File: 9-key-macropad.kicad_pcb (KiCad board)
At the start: 2 copper layers, 20 parts, among them SW1 SW_Push, SW2 SW_Push, SW3 SW_Push, SW4 SW_Push, SW5 SW_Push, SW6 SW_Push, SW7 SW_Push, SW8 SW_Push, SW9 SW_Push, U1 XIAO-RP2040-DIP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

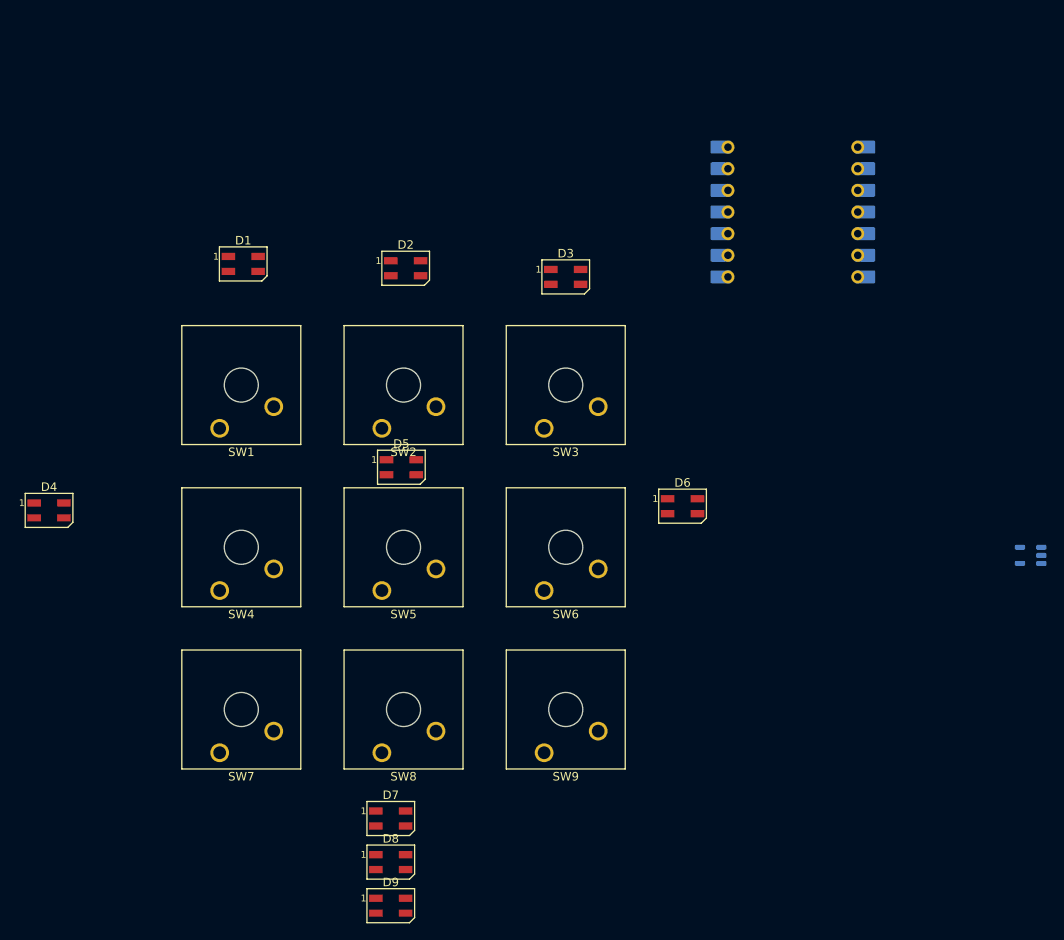
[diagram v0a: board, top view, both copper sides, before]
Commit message: Update switch and LED positions on PCB
Repositioned Cherry MX switches and SK6812MINI LEDs to new coordinates and orientations on the 9-key macropad PCB. This change likely reflects a new layout or mechanical design for improved ergonomics or aesthetics.
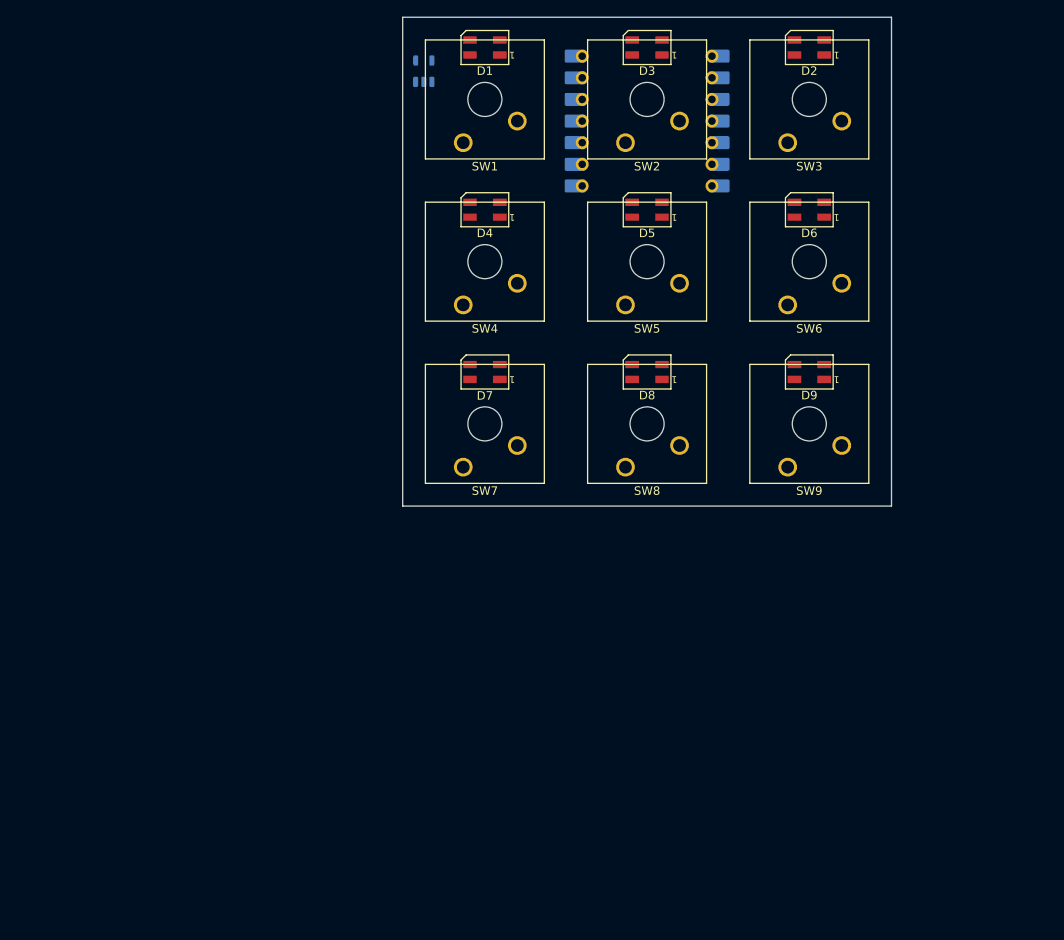
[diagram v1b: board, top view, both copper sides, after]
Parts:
- moved U2 91.2 mm to (72.2, 77.4), turned to 90 degrees
- moved D9 79.7 mm to (117.5, 112.8), turned to 180 degrees
- moved D8 65.0 mm to (98.5, 112.8), turned to 180 degrees
- moved D4 62.2 mm to (79.4, 93.7), turned to 180 degrees
- moved D2 54.0 mm to (117.5, 74.7), turned to 180 degrees
- moved D7 53.6 mm to (79.4, 112.8), turned to 180 degrees
- moved SW1 44.1 mm to (76.9, 85.8)
- moved SW4 44.1 mm to (76.9, 104.9)
- moved SW2 44.1 mm to (95.9, 85.8)
- moved SW3 44.1 mm to (115.0, 85.8)
- moved SW5 44.1 mm to (95.9, 104.9)
- moved SW6 44.1 mm to (115.0, 104.9)
- moved SW7 44.1 mm to (76.9, 123.9)
- moved SW8 44.1 mm to (95.9, 123.9)
- moved SW9 44.1 mm to (115.0, 123.9)
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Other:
- board outline added: 57.4 x 57.4 mm

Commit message: Rearrange key switches and LEDs, update net assignments
Moved key switches and SK6812MINI LEDs to new positions for improved layout. Updated net assignments for GPIO pins to match new key mapping and corrected NEOPIX and unconnected net references. Adjusted footprint locations for U1 and U2 to align with the new design.
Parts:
- moved SW1 19.6 mm to (78.1, 105.4)
- moved SW2 19.6 mm to (97.1, 105.4)
- moved SW3 19.6 mm to (116.2, 105.4)
- moved SW7 19.6 mm to (78.1, 143.5)
- moved SW8 19.6 mm to (97.1, 143.5)
- moved SW9 19.6 mm to (116.2, 143.5)
- moved D1 19.6 mm to (80.6, 94.2)
- moved D2 19.6 mm to (118.7, 94.2)
- moved D3 19.6 mm to (99.7, 94.2)
- moved D4 19.6 mm to (80.6, 113.2)
- moved D5 19.6 mm to (99.7, 113.2)
- moved D6 19.6 mm to (118.7, 113.2)
- moved D7 19.6 mm to (80.6, 132.3)
- moved D8 19.6 mm to (99.7, 132.3)
- moved D9 19.6 mm to (118.7, 132.3)
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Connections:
- U1 pad 1: KEY1 -> unconnected-(U1-GPIO26/ADC0/A0-Pad1)
- U1 pad 10: KEY9 -> KEY1
- U1 pad 11: unconnected-(U1-GPIO3/MOSI-Pad11) -> NEOPIX
- U1 pad 13: unconnected-(U1-GND-Pad13) -> GNDD
- U1 pad 2: KEY2 -> KEY3
- U1 pad 3: KEY3 -> KEY6
- U1 pad 4: KEY4 -> KEY9
- U1 pad 5: KEY5 -> KEY8
- U1 pad 6: KEY6 -> KEY5
- U1 pad 7: NEOPIX -> KEY2
- U1 pad 9: KEY8 -> KEY4
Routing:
- net KEY8: track 0.00 -> 52.6 mm
- net KEY9: track 0.00 -> 46.5 mm
- net KEY7: track 0.00 -> 42.5 mm
- net KEY5: track 0.00 -> 30.9 mm
- net KEY6: track 0.00 -> 27.8 mm
- net KEY4: track 0.00 -> 26.0 mm
- net VCC: track 0.00 -> 17.9 mm
- net KEY1: track 0.00 -> 14.0 mm
- net KEY2: track 0.00 -> 12.3 mm
- net KEY3: track 0.00 -> 12.2 mm
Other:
- board size 57.4 x 57.4 mm -> 57.2 x 57.2 mm

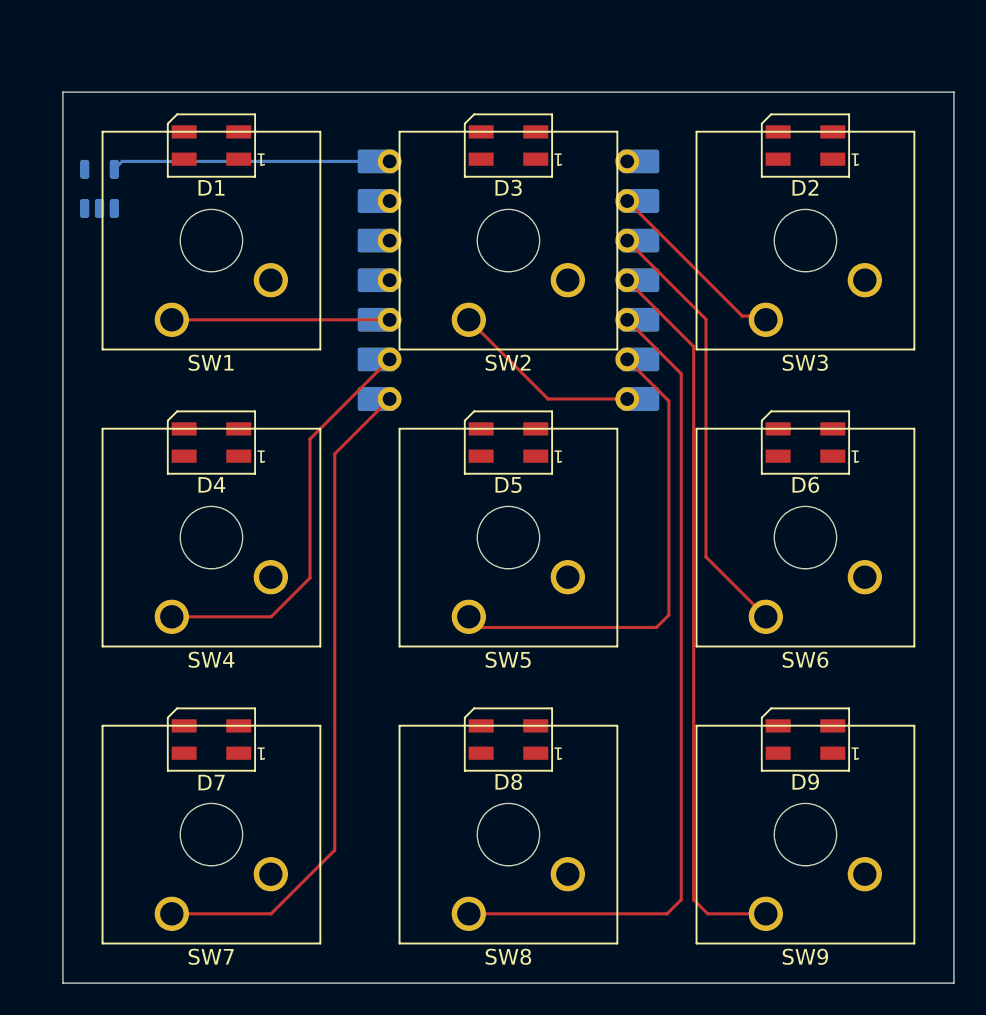
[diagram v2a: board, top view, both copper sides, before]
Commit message: Continued Board Development
Reworked Schematic for better trace layout and started adding traces to PCB design
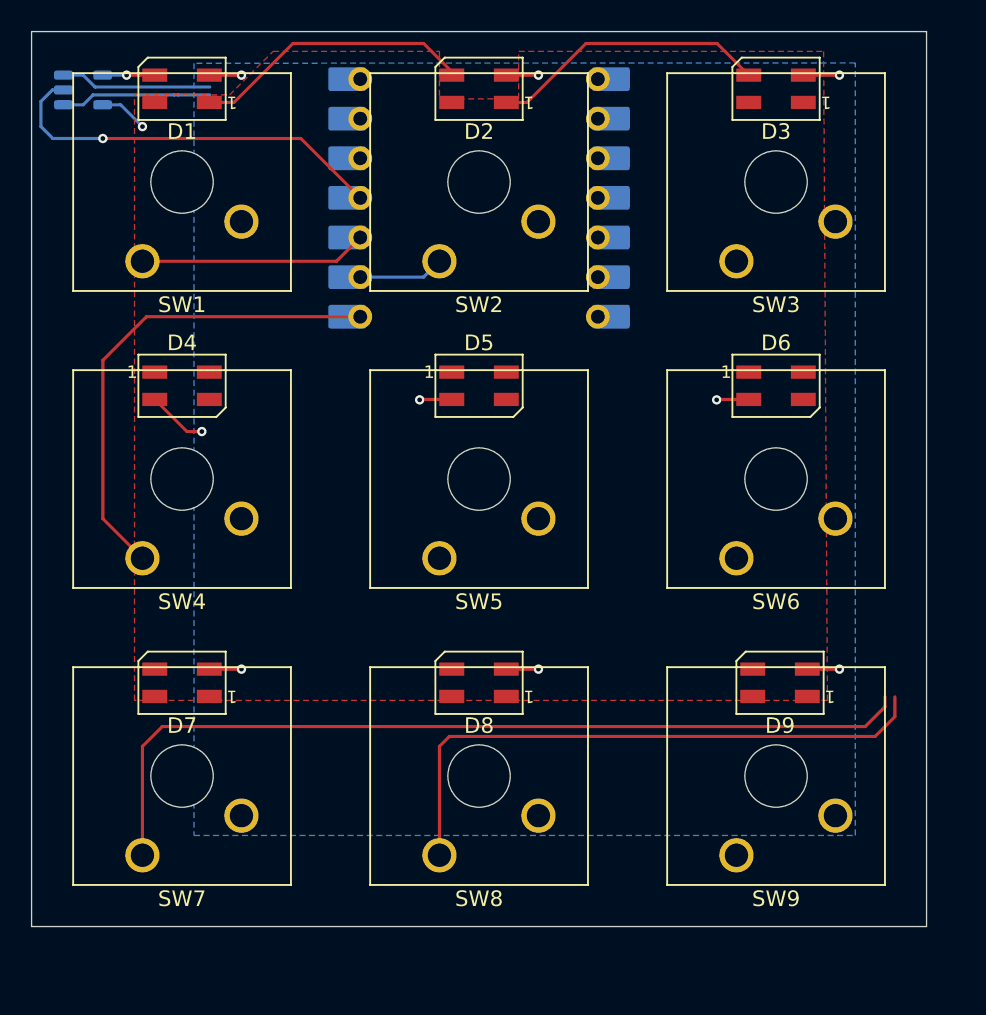
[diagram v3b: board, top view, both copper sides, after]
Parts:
- moved D2 21.2 mm to (97.8, 90.5)
- moved D3 17.5 mm to (116.8, 90.5)
- moved U2 6.43 mm to (72.4, 90.6), turned to 0 degrees
- moved U1 5.61 mm to (97.8, 97.5)
- moved SW8 4.20 mm to (95.2, 139.7)
- moved SW9 4.20 mm to (114.3, 139.7)
- moved SW7 4.20 mm to (76.2, 139.7)
- moved SW2 4.20 mm to (95.2, 101.6)
- moved SW3 4.20 mm to (114.3, 101.6)
- moved SW1 4.20 mm to (76.2, 101.6)
- moved SW5 4.20 mm to (95.2, 120.7)
- moved SW6 4.20 mm to (114.3, 120.7)
- moved SW4 4.20 mm to (76.2, 120.7)
- moved D1 4.10 mm to (78.7, 90.5)
- moved D4 4.10 mm to (78.7, 109.6), turned to 0 degrees
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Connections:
- D4 pad 3: Net-(D3-DOUT) -> Net-(D4-DIN)
- D5 pad 1: Net-(D5-DOUT) -> Net-(D4-DIN)
- D5 pad 3: Net-(D4-DOUT) -> Net-(D5-DIN)
- D6 pad 1: Net-(D6-DOUT) -> Net-(D5-DIN)
- D6 pad 3: Net-(D5-DOUT) -> Net-(D3-DOUT)
- D7 pad 3: Net-(D6-DOUT) -> Net-(D4-DOUT)
- U1 pad 2: KEY3 -> KEY8
- U1 pad 5: KEY8 -> KEY3
- U1 pad 7: KEY2 -> unconnected-(U1-GPIO0/TX-Pad7)
- U1 pad 8: KEY7 -> KEY4
- U1 pad 9: KEY4 -> KEY2
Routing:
- net KEY9: track 46.5 -> 0.00 mm
- net GNDD: track 0.00 -> 40.0 mm, vias 0 -> 9
- net KEY5: track 30.9 -> 0.00 mm
- net KEY6: track 27.8 -> 0.00 mm
- net NEOPIX: track 0.00 -> 25.7 mm, vias 0 -> 1
- net Net-(D1-DOUT): track 0.00 -> 18.1 mm
- net Net-(D2-DOUT): track 0.00 -> 18.0 mm
- net VCC: track 17.9 -> 3.14 mm, vias 0 -> 1
- net KEY8: track 52.6 -> 38.3 mm
- net KEY7: track 42.5 -> 56.3 mm
- net KEY3: track 12.2 -> 0.00 mm
- net KEY2: track 12.3 -> 5.50 mm
- net KEY4: track 26.0 -> 31.4 mm
- net NEOPIX_5V: track 0.00 -> 3.34 mm, vias 0 -> 1
- net KEY1: track 14.0 -> 14.6 mm
- added copper zone on B.Cu, net GNDD
- added copper zone on F.Cu, net VCC
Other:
- board size 57.2 x 57.2 mm -> 57.4 x 57.4 mm

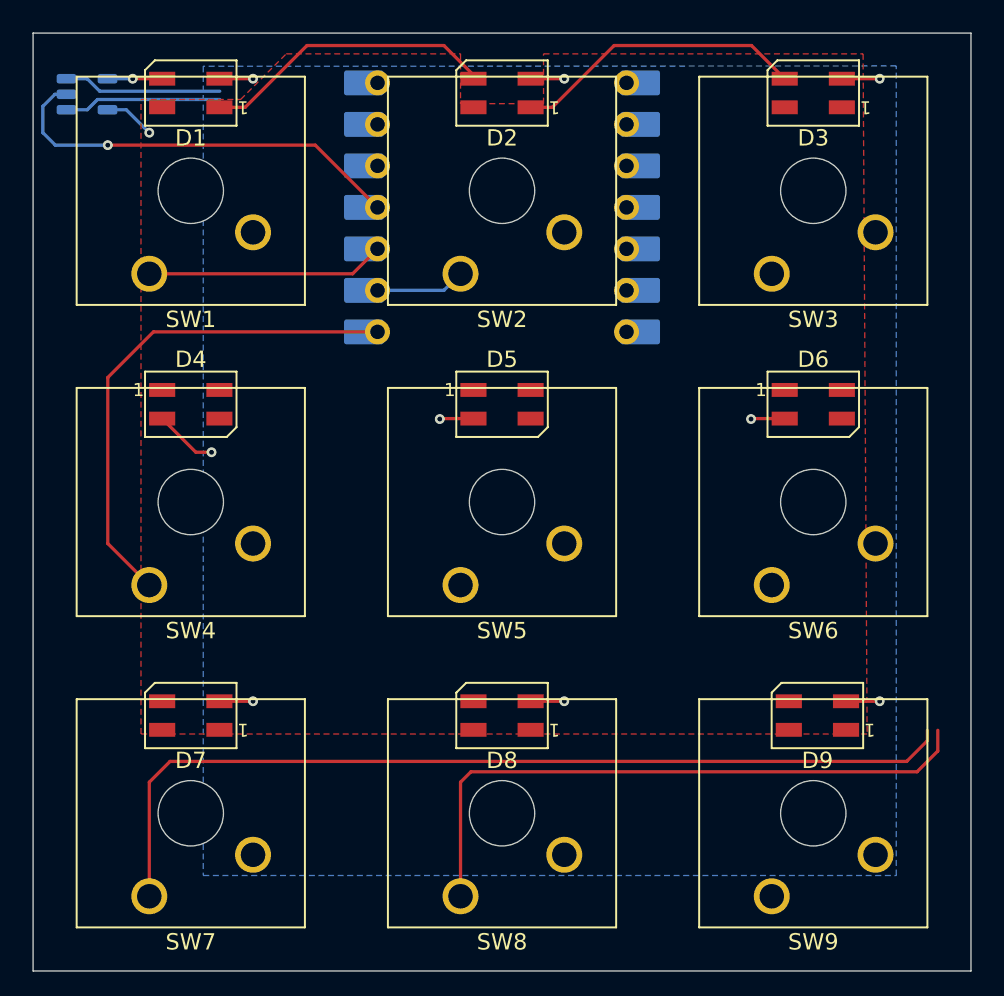
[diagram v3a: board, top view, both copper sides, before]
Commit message: Update net assignments and LED footprints
Reorganized net numbers and names for clarity and consistency, updated LED SK6812MINI footprints and pad orientations, and corrected net connections for keys and LEDs. These changes improve schematic and PCB alignment and resolve mismatches in net assignments.
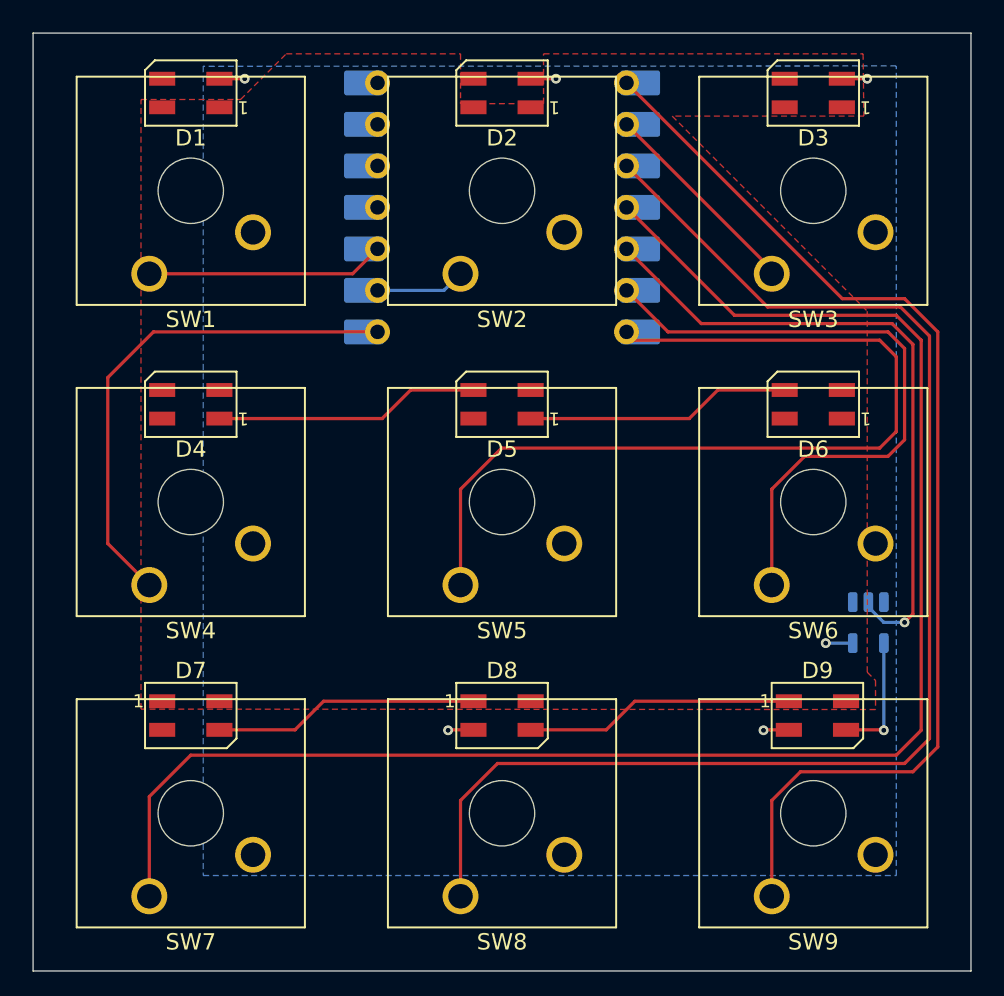
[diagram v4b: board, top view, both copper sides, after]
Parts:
- moved U2 57.7 mm to (120.2, 123.0), turned to -90 degrees
- turned D4 to 180 degrees
- turned D5 to 180 degrees
- turned D6 to 180 degrees
- turned D7 to 0 degrees
- turned D8 to 0 degrees
- turned D9 to 0 degrees
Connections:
- D1 pad 1: Net-(D1-DOUT) -> unconnected-(D1-DOUT-Pad1)
- D1 pad 3: NEOPIX_5V -> unconnected-(D1-DIN-Pad3)
- D2 pad 1: Net-(D2-DOUT) -> unconnected-(D2-DOUT-Pad1)
- D2 pad 3: Net-(D1-DOUT) -> unconnected-(D2-DIN-Pad3)
- D3 pad 1: Net-(D3-DOUT) -> unconnected-(D3-DOUT-Pad1)
- D3 pad 3: Net-(D2-DOUT) -> unconnected-(D3-DIN-Pad3)
- D5 pad 1: Net-(D4-DIN) -> Net-(D5-DOUT)
- D5 pad 3: Net-(D5-DIN) -> Net-(D4-DOUT)
- D6 pad 1: Net-(D5-DIN) -> unconnected-(D6-DOUT-Pad1)
- D6 pad 3: Net-(D3-DOUT) -> Net-(D5-DOUT)
- D7 pad 1: Net-(D7-DOUT) -> Net-(D4-DIN)
- D7 pad 3: Net-(D4-DOUT) -> Net-(D7-DIN)
- D8 pad 1: Net-(D8-DOUT) -> Net-(D7-DIN)
- D8 pad 3: Net-(D7-DOUT) -> Net-(D8-DIN)
- D9 pad 1: unconnected-(D9-DOUT-Pad1) -> Net-(D8-DIN)
- D9 pad 3: Net-(D8-DOUT) -> NEOPIX_5V
- U1 pad 1: unconnected-(U1-GPIO26/ADC0/A0-Pad1) -> KEY9
- U1 pad 11: NEOPIX -> unconnected-(U1-GPIO3/MOSI-Pad11)
- U1 pad 2: KEY8 -> KEY3
- U1 pad 3: KEY6 -> KEY8
- U1 pad 4: KEY9 -> KEY7
- U1 pad 5: KEY3 -> NEOPIX
- U1 pad 6: KEY5 -> KEY6
- U1 pad 7: unconnected-(U1-GPIO0/TX-Pad7) -> KEY5
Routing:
- net KEY9: track 0.00 -> 68.1 mm
- net KEY5: track 0.00 -> 55.7 mm
- net KEY8: track 38.3 -> 83.6 mm
- net KEY7: track 56.3 -> 100.3 mm
- net KEY6: track 0.00 -> 39.3 mm
- net GNDD: track 40.0 -> 7.78 mm, vias 9 -> 5
- net Net-(D1-DOUT): track 18.1 -> 0.00 mm
- net Net-(D2-DOUT): track 18.0 -> 0.00 mm
- net Net-(D8-DIN): track 0.00 -> 16.5 mm
- net Net-(D7-DIN): track 0.00 -> 16.3 mm
- net Net-(D4-DOUT): track 0.00 -> 16.3 mm
- net Net-(D5-DOUT): track 0.00 -> 16.3 mm
- net NEOPIX: track 25.7 -> 40.1 mm
- net KEY3: track 0.00 -> 12.8 mm
- net NEOPIX_5V: track 3.34 -> 7.66 mm
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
